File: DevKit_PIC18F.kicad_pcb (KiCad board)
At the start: 2 copper layers, 41 x 72 mm, 29 parts, among them J1 PIC_ICSP_ICD, J2 USB_B, J3 5P_UART, J4 RA_PORT, J5 RB_PORT, J6 RD_PORT, J7 RC_PORT, J8 RE_PORT, SW1 SW_RST, X1 16MHz

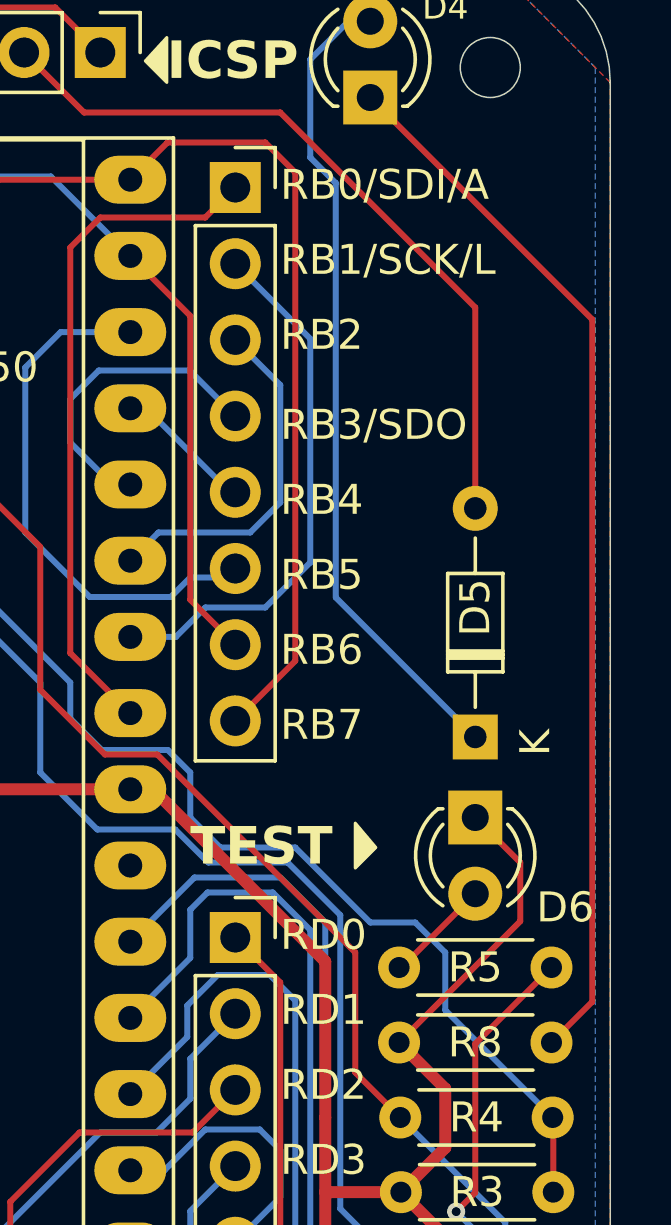
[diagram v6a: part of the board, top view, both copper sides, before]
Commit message: rev.6: fixed LED-D6 -> GND instead VCC pull-up style.
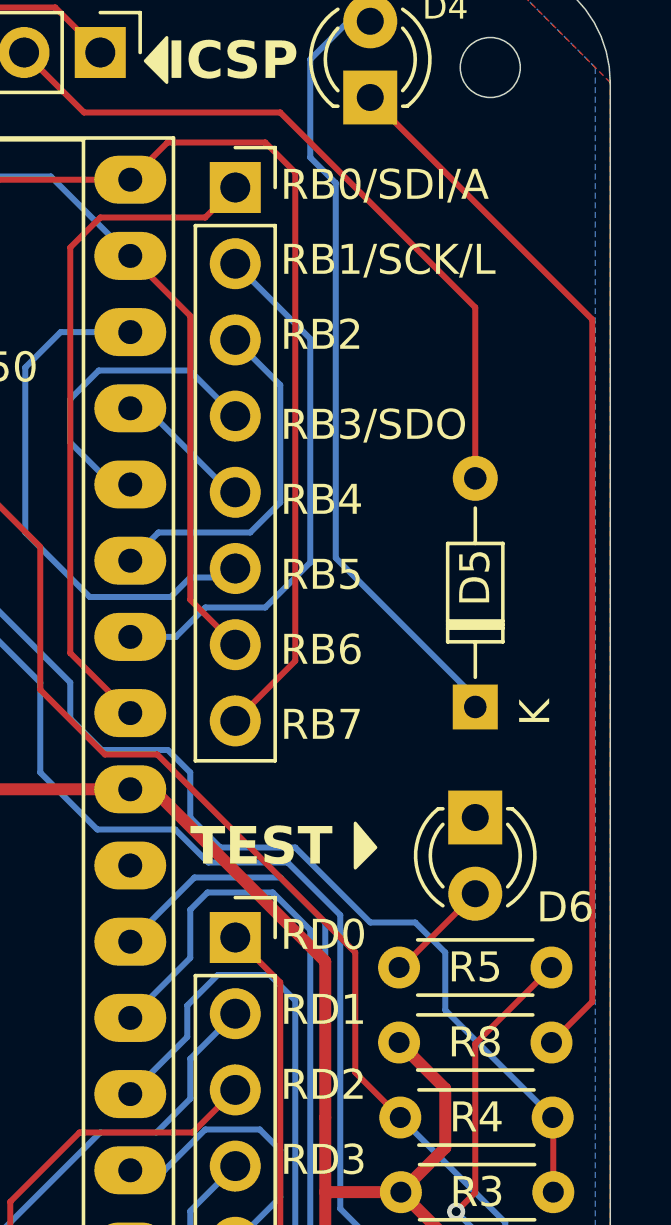
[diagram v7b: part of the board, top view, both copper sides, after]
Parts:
- moved D5 1.00 mm to (104.5, 51.3)
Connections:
- D6 pad 1: VCC -> GND
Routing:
- net VCC: track 125.3 -> 115.5 mm
- net Net-(D5-A): track 25.3 -> 24.3 mm
- net Net-(D4-A): track 27.4 -> 26.4 mm
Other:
- board text added: "DevKit PIC18F45XX Rev.6 : 27th Feb, 2025 Designed by @deulamco"
- board text removed: "DevKit PIC18F45XX Rev.5 : 22th Feb, 2025 Designed by @deulamco"

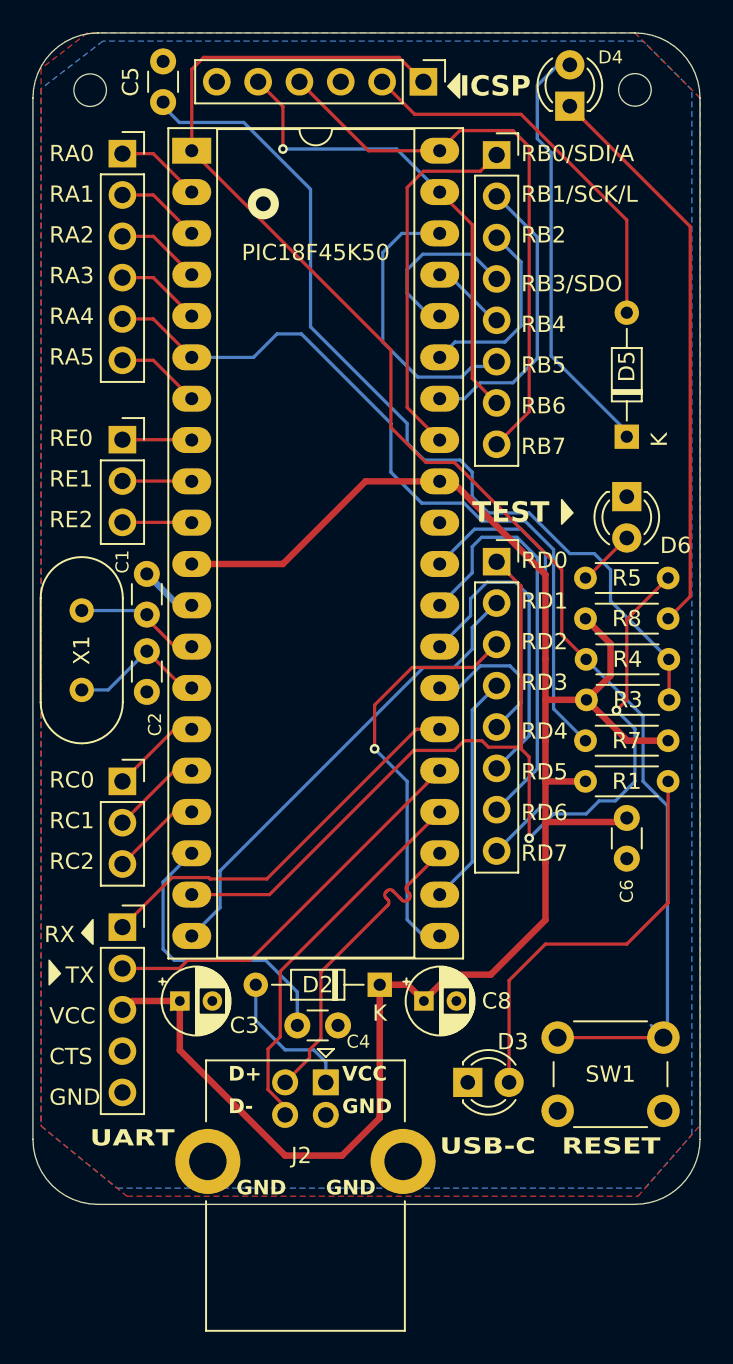
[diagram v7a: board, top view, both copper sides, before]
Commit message: migrate -> KiCAD 9.0.0
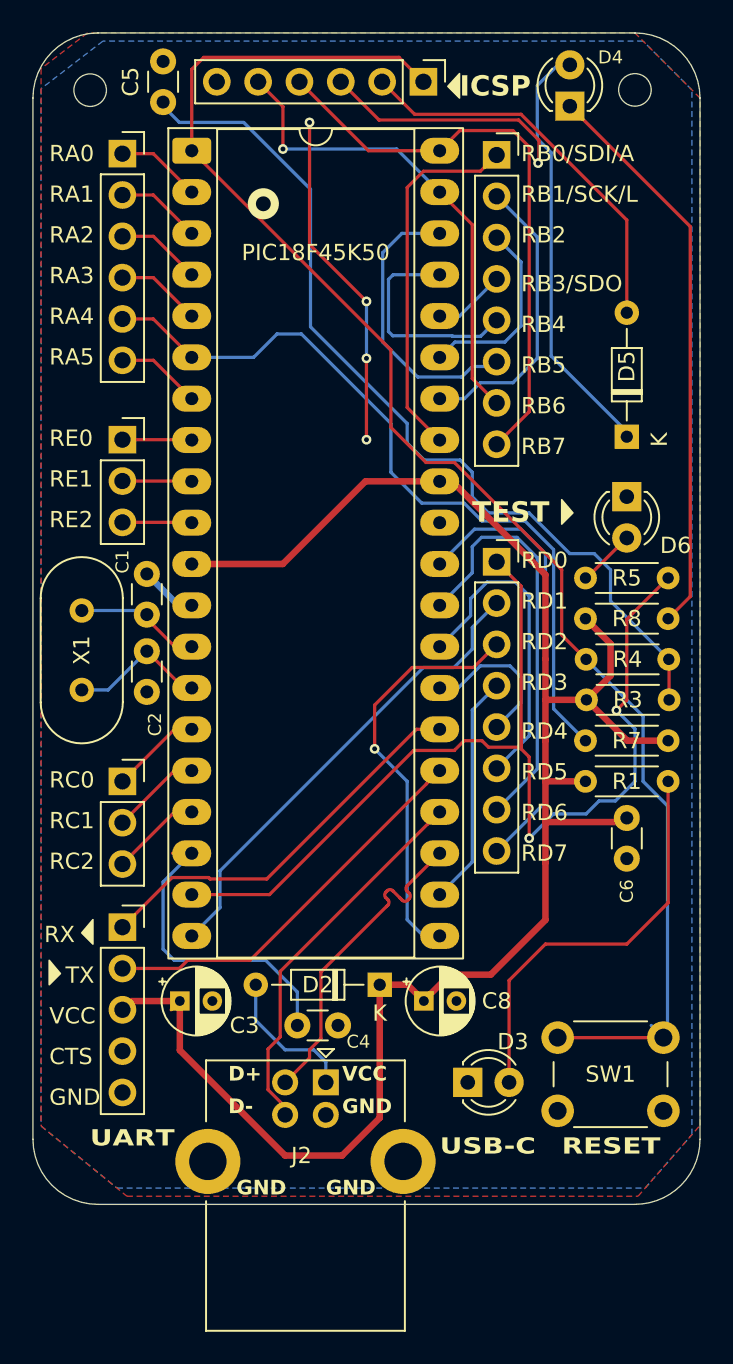
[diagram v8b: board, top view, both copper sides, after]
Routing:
- net GND: track 4.61 -> 40.7 mm, vias 0 -> 5
- net Net-(J5-Pin_5): track 4.66 -> 14.4 mm
- net Net-(J5-Pin_4): track 10.6 -> 5.04 mm
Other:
- board text added: "DevKit PIC18F45XX Rev.7 : 28th Feb, 2025 Designed by @deulamco"
- board text removed: "DevKit PIC18F45XX Rev.6 : 27th Feb, 2025 Designed by @deulamco"
